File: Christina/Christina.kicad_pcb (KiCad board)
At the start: 2 copper layers, 20 parts, among them K1 FINDER-32.21-x300, M1 Motor_DC, M2 Motor_DC, M3 Motor_DC, Q1 BD139, SW1 SW_Push, SW2 SW_Push, U1 74LS386, U2 L7805

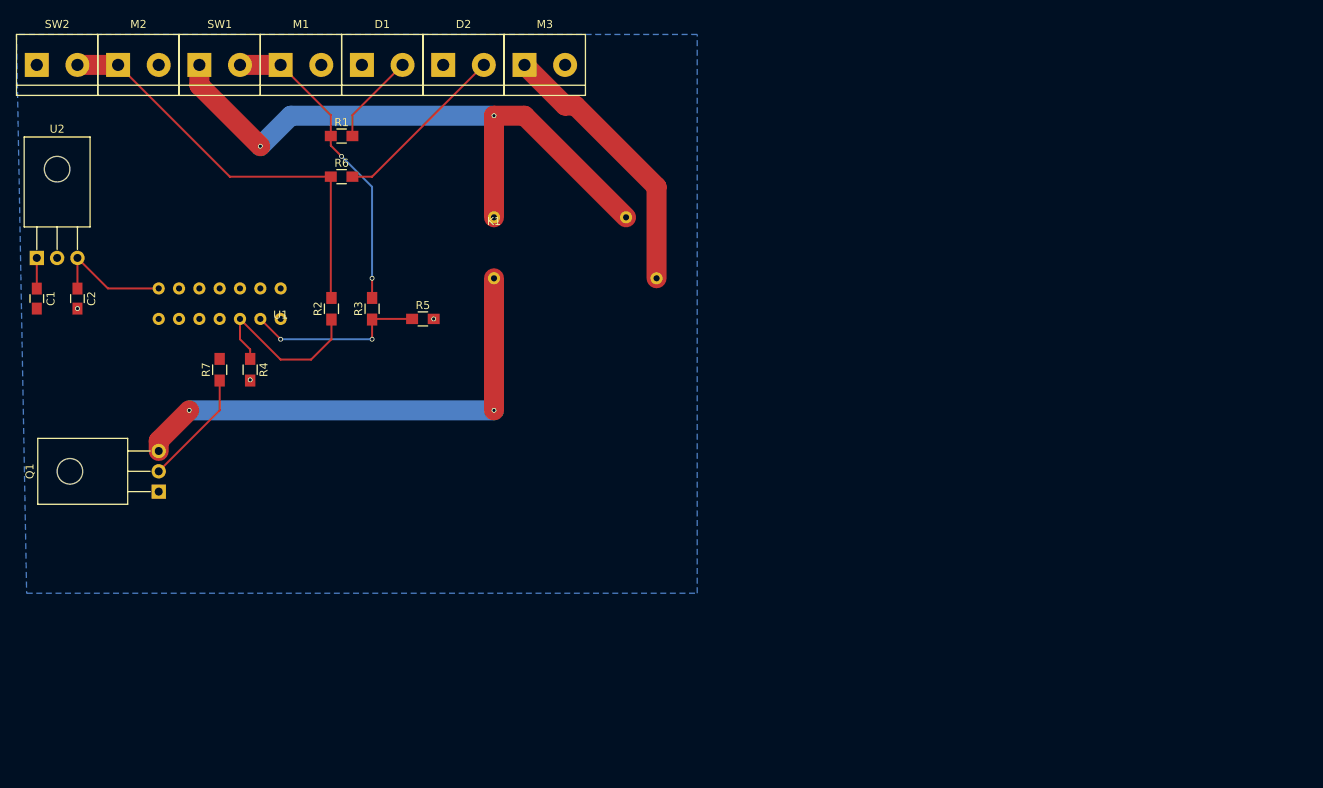
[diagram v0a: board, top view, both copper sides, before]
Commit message: uploaded rerouted board
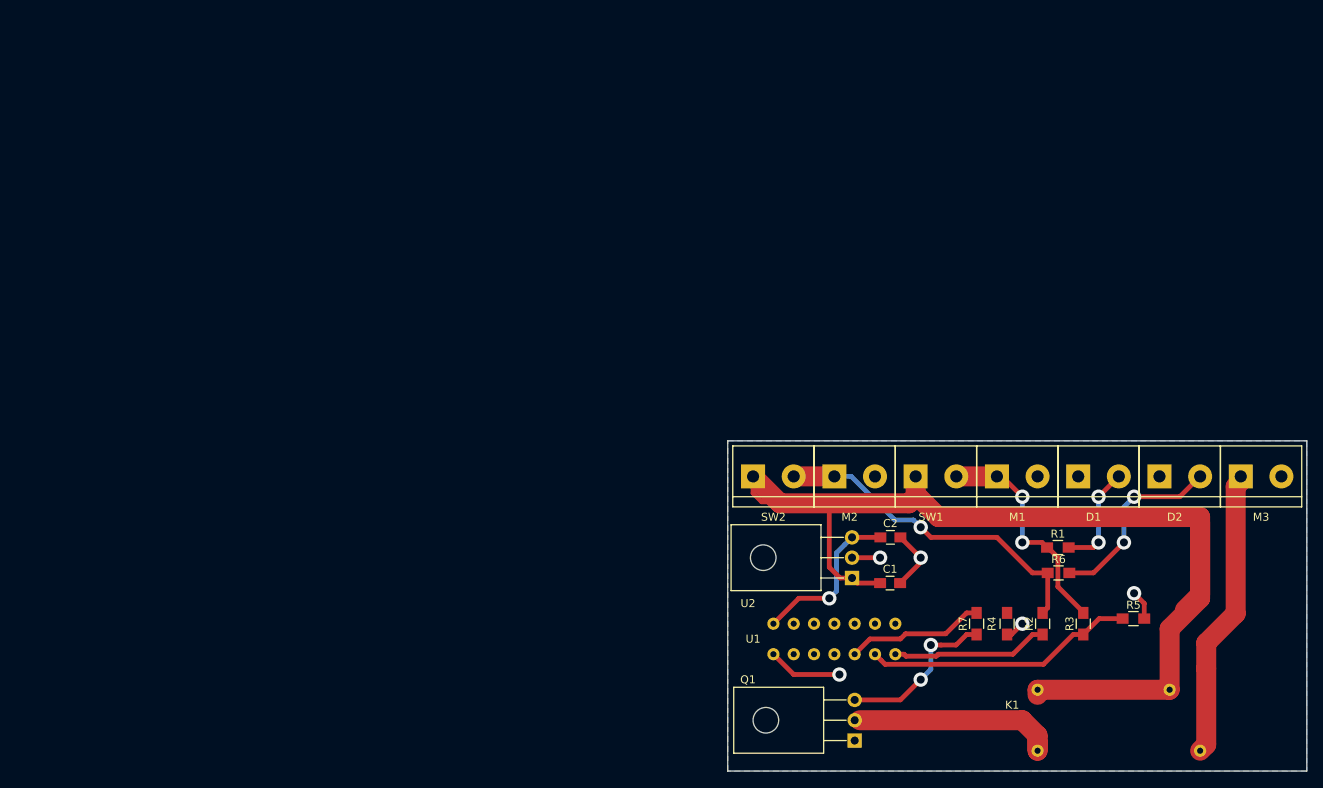
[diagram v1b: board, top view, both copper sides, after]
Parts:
- moved C1 112.4 mm to (121.9, 81.3), turned to 0 degrees
- moved U2 109.5 mm to (117.1, 80.6), turned to 90 degrees
- moved C2 105.9 mm to (121.9, 75.6), turned to 0 degrees
- moved D1 103.3 mm to (145.4, 67.9)
- moved M1 103.3 mm to (135.3, 67.9)
- moved M2 103.3 mm to (114.9, 67.9)
- moved R1 103.3 mm to (142.9, 76.8)
- moved SW1 103.3 mm to (125.1, 67.9)
- moved M3 103.3 mm to (165.7, 67.9)
- moved SW2 103.3 mm to (104.8, 67.9)
- moved D2 103.3 mm to (155.6, 67.9)
- moved R6 102.4 mm to (143.0, 80.0)
- moved R4 99.8 mm to (136.5, 86.4)
- moved R7 99.8 mm to (132.7, 86.4)
- moved R2 97.2 mm to (141.0, 86.4)
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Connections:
- U1 pad 1: GND -> Net-(R2-Pad1)
- U1 pad 3: Net-(R2-Pad1) -> Net-(R7-Pad2)
- U1 pad 4: Net-(R7-Pad2) -> (no net)
- U1 pad 7: (no net) -> GND
- U2 pad 2: Net-(U2-Pad2) -> GND
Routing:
- net (no net): track 0.00 -> 101.6 mm
- net Net-(Q1-Pad3): track 75.8 -> 20.4 mm
- net Net-(K1-Pad11): track 34.3 -> 0.00 mm
- net GND: track 0.18 -> 26.9 mm, vias 10 -> 11
- net +12V: track 82.4 -> 100.7 mm, vias 2 -> 0
- net Net-(R7-Pad2): track 0.00 -> 17.4 mm
- net Net-(R3-Pad1): track 22.5 -> 34.0 mm, vias 2 -> 0
- net Net-(M2-Pad1): track 52.6 -> 42.1 mm, vias 0 -> 1
- net Net-(M1-Pad1): track 38.9 -> 28.5 mm
- net Vcc: track 15.6 -> 20.6 mm, vias 0 -> 1
- net Net-(D1-Pad2): track 11.5 -> 13.3 mm, vias 0 -> 2
- net Net-(R2-Pad1): track 21.4 -> 19.6 mm, vias 0 -> 1
- net Net-(D2-Pad2): track 22.2 -> 24.0 mm, vias 0 -> 2
- net Net-(R4-Pad1): track 1.19 -> 0.00 mm
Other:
- board outline added: 72.4 x 41.3 mm

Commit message: fixed routing, schematic issue
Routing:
- net (no net): track 101.6 -> 0.00 mm
- net +12V: track 100.7 -> 140.4 mm
- net Net-(K1-Pad11): track 0.00 -> 35.8 mm
- net Net-(K1-PadA2): track 0.00 -> 26.2 mm
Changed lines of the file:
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@@
   (page A4)
   (layers
-    (0 F.Cu signal)
-    (31 B.Cu signal)
+    (0 F.Cu signal hide)
+    (31 B.Cu signal hide)
     (32 B.Adhes user)
     (33 F.Adhes user)
@@
   )
   (setup
-    (last_trace_width 2.5)
+    (last_trace_width 0.25)
     (user_trace_width 0.6)
     (user_trace_width 2.5)
@@
   (gr_line (start 173.99 63.5) (end 173.99 104.775) (layer Edge.Cuts) (width 0.15))
   (gr_line (start 101.6 63.5) (end 173.99 63.5) (layer Edge.Cuts) (width 0.15))
-  (segment (start 138.43 98.425) (end 118.11 98.425) (width 2.5) (layer F.Cu) (net 0))
-  (segment (start 140.335 100.33) (end 138.43 98.425) (width 2.5) (layer F.Cu) (net 0))
-  (segment (start 140.335 102.235) (end 140.335 100.33) (width 2.5) (layer F.Cu) (net 0))
-  (segment (start 165.1 69.215) (end 165.735 68.58) (width 2.5) (layer F.Cu) (net 0))
-  (segment (start 165.1 85.09) (end 165.1 69.215) (width 2.5) (layer F.Cu) (net 0))
-  (segment (start 161.416999 88.773001) (end 165.1 85.09) (width 2.5) (layer F.Cu) (net 0))
-  (segment (start 161.416999 91.948001) (end 161.416999 88.773001) (width 2.5) (layer F.Cu) (net 0))
-  (segment (start 160.655 83.185) (end 160.655 73.66) (width 2.5) (layer F.Cu) (net 0))
-  (segment (start 156.845 86.995) (end 160.655 83.185) (width 2.5) (layer F.Cu) (net 0))
-  (segment (start 140.335 94.615) (end 140.335 95.25) (width 2.5) (layer F.Cu) (net 0))
-  (segment (start 160.655 102.235) (end 161.416999 101.473001) (width 2.5) (layer F.Cu) (net 0))
-  (segment (start 161.416999 101.473001) (end 161.416999 91.948001) (width 2.5) (layer F.Cu) (net 0))
-  (segment (start 140.335 102.235) (end 140.335 100.965) (width 2.5) (layer F.Cu) (net 0))
-  (segment (start 156.845 94.615) (end 156.845 86.995) (width 2.5) (layer F.Cu) (net 0))
-  (segment (start 140.335 94.615) (end 156.845 94.615) (width 2.5) (layer F.Cu) (net 0))
+  (segment (start 160.655 83.185) (end 160.655 73.66) (width 2.5) (layer F.Cu) (net 1))
+  (segment (start 156.845 86.995) (end 160.655 83.185) (width 2.5) (layer F.Cu) (net 1))
+  (segment (start 140.335 94.615) (end 140.335 95.25) (width 2.5) (layer F.Cu) (net 1))
+  (segment (start 156.845 94.615) (end 156.845 86.995) (width 2.5) (layer F.Cu) (net 1))
+  (segment (start 140.335 94.615) (end 156.845 94.615) (width 2.5) (layer F.Cu) (net 1))
   (segment (start 160.655 73.025) (end 160.655 82.750002) (width 2.5) (layer F.Cu) (net 1))
   (segment (start 160.655 82.750002) (end 158.75 84.655002) (width 2.5) (layer F.Cu) (net 1))
@@
   (segment (start 147.32 80.01) (end 151.13 76.2) (width 0.6) (layer F.Cu) (net 5))
   (via (at 151.13 76.2) (size 1.8) (drill 1) (layers F.Cu B.Cu) (net 5))
+  (segment (start 138.43 98.425) (end 118.11 98.425) (width 2.5) (layer F.Cu) (net 6))
+  (segment (start 140.335 100.33) (end 138.43 98.425) (width 2.5) (layer F.Cu) (net 6))
+  (segment (start 140.335 102.235) (end 140.335 100.33) (width 2.5) (layer F.Cu) (net 6))
+  (segment (start 140.335 102.235) (end 140.335 100.965) (width 2.5) (layer F.Cu) (net 6))
   (segment (start 128.272792 89.022011) (end 127 89.022011) (width 0.6) (layer F.Cu) (net 7))
   (segment (start 130.152989 89.022011) (end 128.272792 89.022011) (width 0.6) (layer F.Cu) (net 7))
@@
   (segment (start 128.852999 87.622001) (end 131.465 85.01) (width 0.6) (layer F.Cu) (net 13))
   (segment (start 131.465 85.01) (end 132.715 85.01) (width 0.6) (layer F.Cu) (net 13))
+  (segment (start 165.1 69.215) (end 165.735 68.58) (width 2.5) (layer F.Cu) (net 14))
+  (segment (start 165.1 85.09) (end 165.1 69.215) (width 2.5) (layer F.Cu) (net 14))
+  (segment (start 161.416999 88.773001) (end 165.1 85.09) (width 2.5) (layer F.Cu) (net 14))
+  (segment (start 161.416999 91.948001) (end 161.416999 88.773001) (width 2.5) (layer F.Cu) (net 14))
+  (segment (start 160.655 102.235) (end 161.416999 101.473001) (width 2.5) (layer F.Cu) (net 14))
+  (segment (start 161.416999 101.473001) (end 161.416999 91.948001) (width 2.5) (layer F.Cu) (net 14))
   (zone (net 2) (net_name GND) (layer B.Cu) (hatch edge 0.508)
     (connect_pads (clearance 0.508))
